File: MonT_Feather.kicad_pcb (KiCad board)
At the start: 2 copper layers, 50.8 x 22.9 mm, 12 parts, among them J1 Adafruit_Feather, J2 DB25_Male, U1 MAX3232

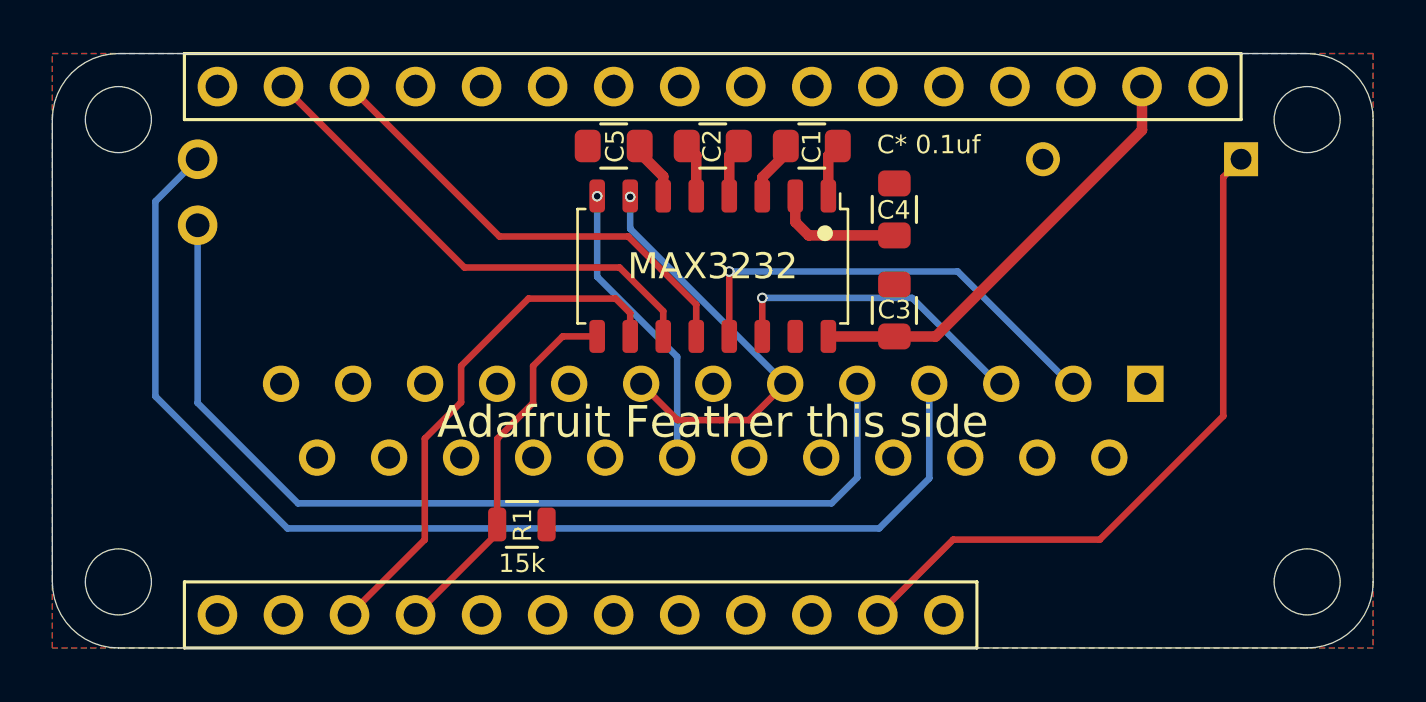
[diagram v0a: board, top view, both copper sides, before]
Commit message: boms and remove dsr pulldown
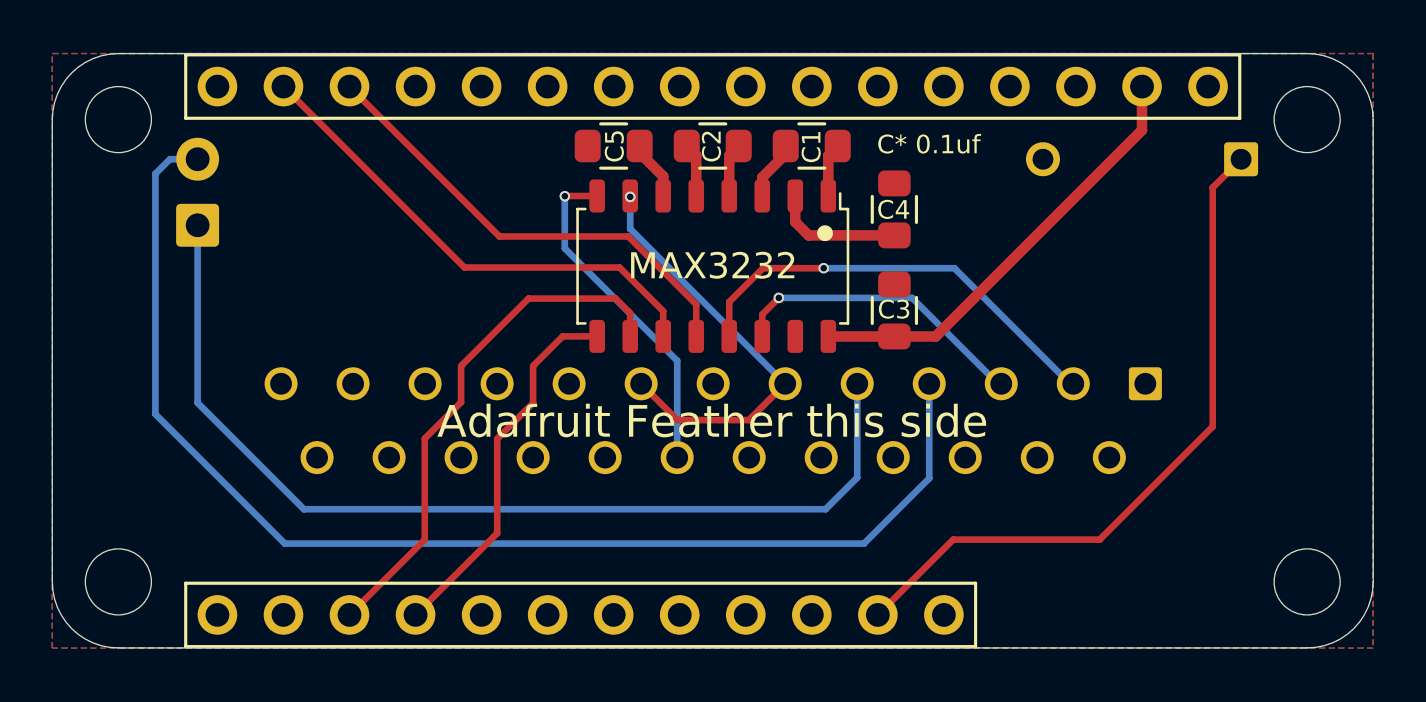
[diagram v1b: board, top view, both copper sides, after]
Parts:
- removed R1: 15k, 0_LOCAL:R_0805
- JP1: footprint 0_LOCAL:JP_H -> 0_LOCAL:PinHeader_1x02_P2.54mm_Horizontal
- moved JP1 1.27 mm to (127.5, 91.7), turned to 0 degrees
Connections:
- JP1 pad 1: /RTS -> /CTS
- JP1 pad 2: /CTS -> /RTS
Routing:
- net /DTR: track 11.3 -> 13.1 mm
- net /RTS: track 46.1 -> 47.6 mm
- net /TXD: track 17.4 -> 16.8 mm
